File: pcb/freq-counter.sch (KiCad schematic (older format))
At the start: 64 parts, among them J1 RPM on board, J10 Power-Terminal0, J11 Hz/RPM_Terminal1, J12 Hz/RPM_Terminal0, J13 1kMG_Terminal1, J14 1kMG_Terminal0, J2 BNC, J3 RPM to Board, J4 Jack-DC, J5 Segments-Terminal0, J6 Digits-Terminal0, J7 Segments-Terminal1, J8 Digits-Terminal1, J9 Power-Terminal1, Q1 CSC388A, Q2 CSC388A, Q3 2SA1015, Q4 2SC1815, Q5 2SC1815, SW1 on/off, SW2 count up, SW3 toggle, SW4 SW_SIGNAL, U1 SN74HC02N, U2 ATTINY4313-PU(freq-counter), U3 EE-SX460, Y1 10MHz

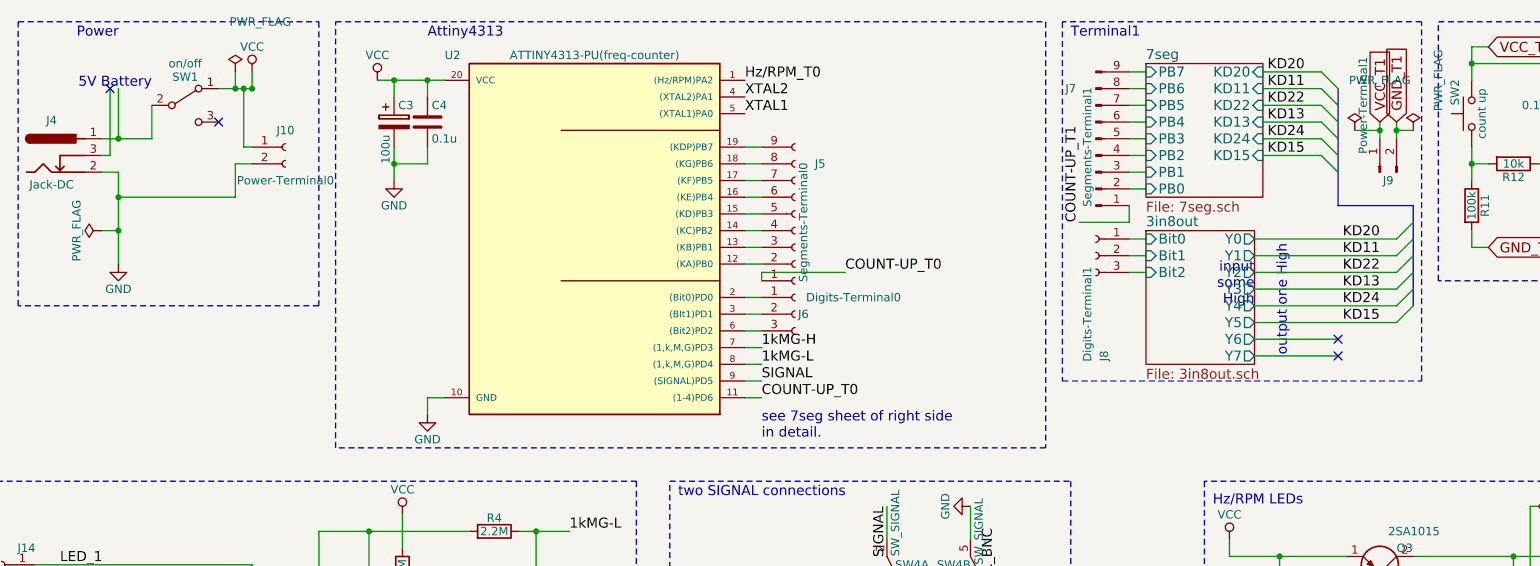
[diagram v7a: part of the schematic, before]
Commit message: Power-Digtis_Terminal1 を作成。Power, Digits の Terminal1 を連結させた。
Connectors_JSTを使っても取り外しを出来るのは，
１階と２階の基板を離してからだと思ったので近くにいた，Digits系と繋げてしまった。
こっちの方が強度を出せると思うため。
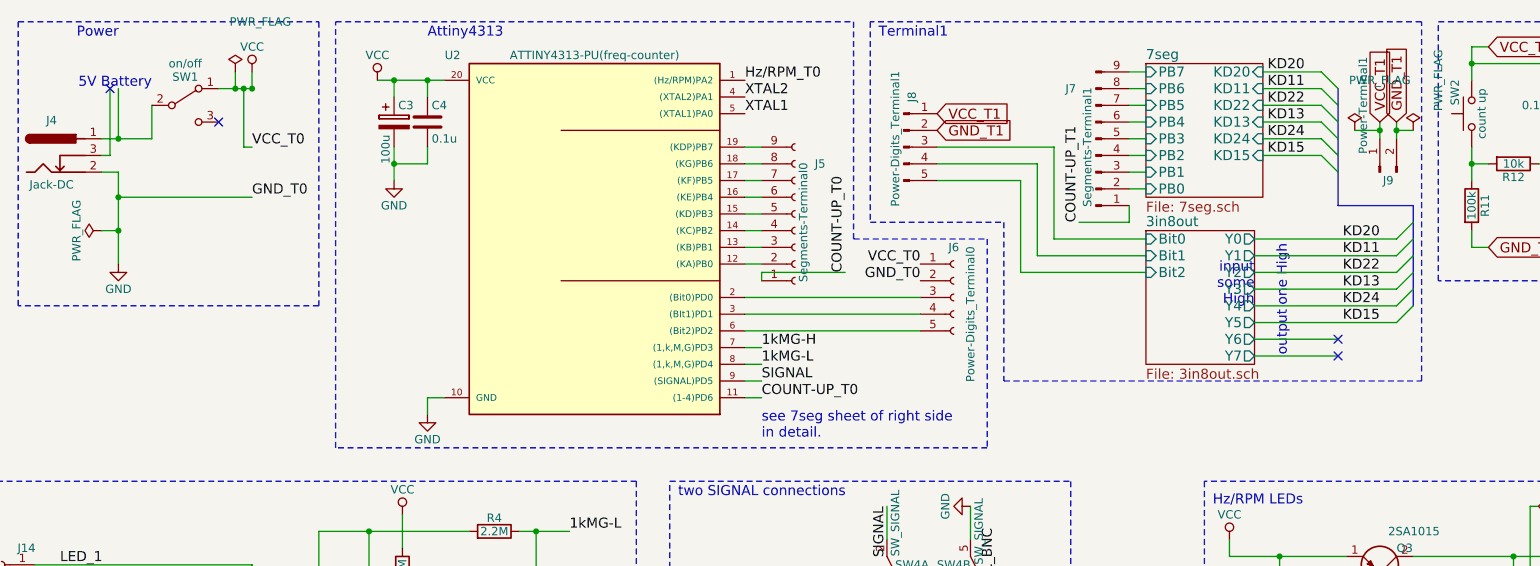
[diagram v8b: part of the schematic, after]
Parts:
- removed J10: Power-Terminal0, Conn_JST:JST_XH_B02B-XH-A_1x02_P2.50mm_Horizontal, symbol Conn_01x02_Female
- removed J6: Digits-Terminal0, Connector_PinSocket_2.54mm:PinSocket_1x03_P2.54mm_Vertical, symbol Conn_01x03_Female
- removed J8: Digits-Terminal1, Connector_PinHeader_2.54mm:PinHeader_1x03_P2.54mm_Vertical, symbol Conn_01x03_Female
- added J6: Power-Digits_Terminal0, Connector_PinSocket_2.54mm:PinSocket_1x05_P2.54mm_Vertical, symbol Conn_01x05_Female
- added J8: Power-Digits_Terminal1, Connector_PinHeader_2.54mm:PinHeader_1x05_P2.54mm_Vertical, symbol Conn_01x05_Male
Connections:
- net 3in8out/Bit0: now also J8.3 (Pin_3)
- net 3in8out/Bit1: now also J8.4 (Pin_4)
- net 3in8out/Bit2: now also J8.5 (Pin_5)
- net GND: now also J6.2 (Pin_2)
- net GND_T1: now also J8.2 (Pin_2)
- net VCC: now also J6.1 (Pin_1)
- net VCC_T1: now also J8.1 (Pin_1)
- net at U2.2 ((Bit0)PD0): now also J6.3 (Pin_3)
- net at U2.3 ((BIt1)PD1): now also J6.4 (Pin_4)
- net at U2.6 ((Bit2)PD2): now also J6.5 (Pin_5)
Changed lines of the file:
@@
 $EndComp
 $Comp
-L GND #PWR01
+L GND #PWR4
 U 1 1 5A10C10B
 P 1450 5100
-F 0 "#PWR01" H 1450 4850 50  0001 C CNN
+F 0 "#PWR4" H 1450 4850 50  0001 C CNN
 F 1 "GND" H 1450 4950 50  0000 C CNN
 F 2 "" H 1450 5100 50  0001 C CNN
@@
 $EndComp
 $Comp
-L GND #PWR02
+L GND #PWR13
 U 1 1 5A102C86
 P 5050 6000
-F 0 "#PWR02" H 5050 5750 50  0001 C CNN
+F 0 "#PWR13" H 5050 5750 50  0001 C CNN
 F 1 "GND" H 5050 5850 50  0000 C CNN
 F 2 "" H 5050 6000 50  0001 C CNN
@@
 $EndComp
 $Comp
-L GND #PWR03
+L GND #PWR3
 U 1 1 5A14ACE7
 P 1250 2200
-F 0 "#PWR03" H 1250 1950 50  0001 C CNN
+F 0 "#PWR3" H 1250 1950 50  0001 C CNN
 F 1 "GND" H 1250 2050 50  0000 C CNN
 F 2 "" H 1250 2200 50  0001 C CNN
@@
 $EndComp
 $Comp
-L PWR_FLAG #FLG04
+L PWR_FLAG #FLG1
 U 1 1 5A14B084
 P 1150 2000
-F 0 "#FLG04" H 1150 2075 50  0001 C CNN
+F 0 "#FLG1" H 1150 2075 50  0001 C CNN
 F 1 "PWR_FLAG" H 1150 2150 50  0000 C CNN
 F 2 "" H 1150 2000 50  0001 C CNN
@@
 $EndComp
 $Comp
-L PWR_FLAG #FLG05
+L PWR_FLAG #FLG2
 U 1 1 5A14B889
 P 1950 1050
-F 0 "#FLG05" H 1950 1125 50  0001 C CNN
+F 0 "#FLG2" H 1950 1125 50  0001 C CNN
 F 1 "PWR_FLAG" H 2100 1350 50  0000 C CNN
 F 2 "" H 1950 1050 50  0001 C CNN
@@
 $EndComp
 $Comp
-L GND #PWR06
+L GND #PWR8
 U 1 1 5A14CF4C
 P 2900 1700
-F 0 "#PWR06" H 2900 1450 50  0001 C CNN
+F 0 "#PWR8" H 2900 1450 50  0001 C CNN
 F 1 "GND" H 2900 1550 50  0000 C CNN
 F 2 "" H 2900 1700 50  0001 C CNN
@@
 Power
 $Comp
-L PWR_FLAG #FLG07
+L PWR_FLAG #FLG4
 U 1 1 5A15C58C
 P 5500 5050
-F 0 "#FLG07" H 5500 5125 50  0001 C CNN
+F 0 "#FLG4" H 5500 5125 50  0001 C CNN
 F 1 "PWR_FLAG" H 5450 5200 50  0000 C CNN
 F 2 "" H 5500 5050 50  0001 C CNN
@@
 $EndComp
 $Comp
-L PWR_FLAG #FLG08
+L PWR_FLAG #FLG3
 U 1 1 5A15C934
 P 5450 5400
-F 0 "#FLG08" H 5450 5475 50  0001 C CNN
+F 0 "#FLG3" H 5450 5475 50  0001 C CNN
 F 1 "PWR_FLAG" V 5350 5400 50  0000 C CNN
 F 2 "" H 5450 5400 50  0001 C CNN
@@
 NoConn ~ 1200 1150
 $Comp
-L VCC #PWR09
+L VCC #PWR5
 U 1 1 5A193502
 P 2050 1050
-F 0 "#PWR09" H 2050 900 50  0001 C CNN
+F 0 "#PWR5" H 2050 900 50  0001 C CNN
 F 1 "VCC" H 2050 1200 50  0000 C CNN
 F 2 "" H 2050 1050 50  0001 C CNN
@@
 Text Label 6400 4500 0    60   ~ 0
 GND_BNC
-$Comp
-L Conn_01x03_Female J6
-U 1 1 5A1E8B3E
-P 5300 2500
-F 0 "J6" H 5350 2500 50  0000 C CNN
-F 1 "Digits-Terminal0" H 5650 2600 50  0000 C CNN
-F 2 "Connector_PinSocket_2.54mm:PinSocket_1x03_P2.54mm_Vertical" H 5300 2500 50  0001 C CNN
-F 3 "" H 5300 2500 50  0001 C CNN
-	1    5300 2500
-	1    0    0    -1
-$EndComp
-$Comp
-L Conn_01x03_Female J8
-U 1 1 5A1EAFDB
-P 7100 2150
-F 0 "J8" V 7050 1550 50  0000 C CNN
-F 1 "Digits-Terminal1" V 7150 1800 50  0000 C CNN
-F 2 "Connector_PinHeader_2.54mm:PinHeader_1x03_P2.54mm_Vertical" H 7100 2150 50  0001 C CNN
-F 3 "" H 7100 2150 50  0001 C CNN
-	1    7100 2150
-	-1   0    0    -1
-$EndComp
-Text Notes 6950 850  0    60   ~ 0
+Text Notes 5800 850  0    60   ~ 0
 Terminal1
 $Comp
@@
 GND_T1
 $Comp
-L Conn_01x02_Female J10
-U 1 1 5A202C49
-P 2250 1500
-F 0 "J10" H 2250 1600 50  0000 C CNN
-F 1 "Power-Terminal0" H 2250 1300 50  0000 C CNN
-F 2 "Conn_JST:JST_XH_B02B-XH-A_1x02_P2.50mm_Horizontal" H 2250 1500 50  0001 C CNN
-F 3 "" H 2250 1500 50  0001 C CNN
-	1    2250 1500
-	1    0    0    -1
-$EndComp
-$Comp
-L VCC #PWR010
+L VCC #PWR7
 U 1 1 5A20AA1B
 P 2800 1100
-F 0 "#PWR010" H 2800 950 50  0001 C CNN
+F 0 "#PWR7" H 2800 950 50  0001 C CNN
 F 1 "VCC" H 2800 1250 50  0000 C CNN
 F 2 "" H 2800 1100 50  0001 C CNN
@@
 VCC_T1
 $Comp
-L PWR_FLAG #FLG011
+L PWR_FLAG #FLG6
 U 1 1 5A1E7BBB
 P 9000 1400
-F 0 "#FLG011" H 9000 1475 50  0001 C CNN
+F 0 "#FLG6" H 9000 1475 50  0001 C CNN
 F 1 "PWR_FLAG" V 9150 1700 50  0000 C CNN
 F 2 "" H 9000 1400 50  0001 C CNN
@@
 $EndComp
 $Comp
-L PWR_FLAG #FLG012
+L PWR_FLAG #FLG5
 U 1 1 5A1E8382
 P 8650 1400
-F 0 "#FLG012" H 8650 1475 50  0001 C CNN
+F 0 "#FLG5" H 8650 1475 50  0001 C CNN
 F 1 "PWR_FLAG" H 8800 1700 50  0000 C CNN
 F 2 "" H 8650 1400 50  0001 C CNN
@@
 $EndComp
 $Comp
-L VCC #PWR013
+L VCC #PWR2
 U 1 1 5A1EAB1C
 P 1000 4500
-F 0 "#PWR013" H 1000 4350 50  0001 C CNN
+F 0 "#PWR2" H 1000 4350 50  0001 C CNN
 F 1 "VCC" H 1000 4650 50  0000 C CNN
 F 2 "" H 1000 4500 50  0001 C CNN
@@
 $EndComp
 $Comp
-L GND #PWR014
+L GND #PWR11
 U 1 1 5A1EBF20
 P 3100 3100
-F 0 "#PWR014" H 3100 2850 50  0001 C CNN
+F 0 "#PWR11" H 3100 2850 50  0001 C CNN
 F 1 "GND" H 3100 2950 50  0000 C CNN
 F 2 "" H 3100 3100 50  0001 C CNN
@@
 $EndComp
 $Comp
-L GND #PWR015
+L GND #PWR6
 U 1 1 5A1ECBC1
 P 2450 6400
-F 0 "#PWR015" H 2450 6150 50  0001 C CNN
+F 0 "#PWR6" H 2450 6150 50  0001 C CNN
 F 1 "GND" H 2450 6250 50  0000 C CNN
 F 2 "" H 2450 6400 50  0001 C CNN
@@
 $EndComp
 $Comp
-L GND #PWR016
+L GND #PWR1
 U 1 1 5A1ED93F
 P 850 4550
-F 0 "#PWR016" H 850 4300 50  0001 C CNN
+F 0 "#PWR1" H 850 4300 50  0001 C CNN
 F 1 "GND" H 850 4400 50  0000 C CNN
 F 2 "" H 850 4550 50  0001 C CNN
@@
 $EndComp
 $Comp
-L GND #PWR017
+L GND #PWR10
 U 1 1 5A1EE509
 P 2950 4800
-F 0 "#PWR017" H 2950 4550 50  0001 C CNN
+F 0 "#PWR10" H 2950 4550 50  0001 C CNN
 F 1 "GND" H 2950 4650 50  0000 C CNN
 F 2 "" H 2950 4800 50  0001 C CNN
@@
 $EndComp
 $Comp
-L VCC #PWR018
+L VCC #PWR12
 U 1 1 5A1EEDD1
 P 3100 5250
-F 0 "#PWR018" H 3100 5100 50  0001 C CNN
+F 0 "#PWR12" H 3100 5100 50  0001 C CNN
 F 1 "VCC" H 3100 5400 50  0000 C CNN
 F 2 "" H 3100 5250 50  0001 C CNN
@@
 $EndComp
 $Comp
-L VCC #PWR019
+L VCC #PWR9
 U 1 1 5A1EFB20
 P 2950 3700
-F 0 "#PWR019" H 2950 3550 50  0001 C CNN
+F 0 "#PWR9" H 2950 3550 50  0001 C CNN
 F 1 "VCC" H 2950 3850 50  0000 C CNN
 F 2 "" H 2950 3700 50  0001 C CNN
@@
 $EndComp
 $Comp
-L GND #PWR020
+L GND #PWR17
 U 1 1 5A1F0879
 P 7900 6150
-F 0 "#PWR020" H 7900 5900 50  0001 C CNN
+F 0 "#PWR17" H 7900 5900 50  0001 C CNN
 F 1 "GND" H 7900 6000 50  0000 C CNN
 F 2 "" H 7900 6150 50  0001 C CNN
@@
 $EndComp
 $Comp
-L VCC #PWR021
+L VCC #PWR16
 U 1 1 5A1F0C13
 P 7900 3850
-F 0 "#PWR021" H 7900 3700 50  0001 C CNN
+F 0 "#PWR16" H 7900 3700 50  0001 C CNN
 F 1 "VCC" H 7900 4000 50  0000 C CNN
 F 2 "" H 7900 3850 50  0001 C CNN
@@
 $EndComp
 $Comp
-L GND #PWR022
+L GND #PWR15
 U 1 1 5A1F3CDE
 P 6350 3650
-F 0 "#PWR022" H 6350 3400 50  0001 C CNN
+F 0 "#PWR15" H 6350 3400 50  0001 C CNN
 F 1 "GND" H 6350 3500 50  0000 C CNN
 F 2 "" H 6350 3650 50  0001 C CNN
@@
 $EndComp
 $Comp
-L VCC #PWR023
+L VCC #PWR14
 U 1 1 5A1F4C25
 P 5800 4400
-F 0 "#PWR023" H 5800 4250 50  0001 C CNN
+F 0 "#PWR14" H 5800 4250 50  0001 C CNN
 F 1 "VCC" H 5800 4550 50  0000 C CNN
 F 2 "" H 5800 4400 50  0001 C CNN
@@
 	5000 2700 5100 2700
 Wire Wire Line
-	7300 2250 7400 2250
-Wire Wire Line
-	7300 2050 7400 2050
-Wire Wire Line
-	7300 2150 7400 2150
+	6650 2250 7400 2250
+Wire Wire Line
+	6850 2050 7400 2050
+Wire Wire Line
+	6750 2150 7400 2150
 Wire Wire Line
 	7300 1750 7400 1750
@@
 	9350 2000 9350 2100
 Wire Notes Line
-	6800 3300 2550 3300
+	6450 3300 2550 3300
 Wire Notes Line
 	2550 3300 2550 750
 Wire Notes Line
-	2550 750  6800 750
-Wire Notes Line
-	6800 750  6800 3300
+	2550 750  5650 750
 Wire Wire Line
 	5250 6400 5200 6400
@@
 	5000 2200 5100 2200
 Wire Wire Line
-	5100 2400 5000 2400
-Wire Wire Line
-	5000 2500 5100 2500
-Wire Wire Line
-	5100 2600 5000 2600
+	6050 2400 5000 2400
+Wire Wire Line
+	5000 2500 6050 2500
+Wire Wire Line
+	6050 2600 5000 2600
 Wire Wire Line
 	8550 2750 8050 2750
 Wire Notes Line
-	6900 750  6900 2900
-Wire Notes Line
-	6900 2900 9050 2900
+	6550 2900 9050 2900
 Wire Notes Line
 	9050 2900 9050 750
 Wire Notes Line
-	9050 750  6900 750
+	9050 750  5750 750
 Wire Wire Line
 	8800 1350 8800 1450
@@
 Connection ~ 2000 1150
 Wire Wire Line
-	2050 1600 1950 1600
-Wire Wire Line
-	1950 1600 1950 1800
-Wire Wire Line
-	1950 1800 1250 1800
+	1250 1800 2050 1800
 Connection ~ 1250 1800
 Wire Wire Line
@@
 Text Label 5100 3000 0    60   ~ 0
 COUNT-UP_T0
-Text Label 5600 2250 0    60   ~ 0
+Text Label 5600 2250 1    60   ~ 0
 COUNT-UP_T0
 Wire Wire Line
@@
 Wire Wire Line
 	2250 5700 2250 5500
+$Comp
+L Conn_01x05_Female J6
+U 1 1 5A237074
+P 6250 2400
+F 0 "J6" H 6250 2700 50  0000 C CNN
+F 1 "Power-Digits_Terminal0" V 6350 2300 50  0000 C CNN
+F 2 "Connector_PinSocket_2.54mm:PinSocket_1x05_P2.54mm_Vertical" H 6250 2400 50  0001 C CNN
+F 3 "" H 6250 2400 50  0001 C CNN
+	1    6250 2400
+	1    0    0    -1
+$EndComp
+Text Label 2050 1500 0    60   ~ 0
+VCC_T0
+Text Label 2050 1800 0    60   ~ 0
+GND_T0
+Text Label 6050 2200 2    60   ~ 0
+VCC_T0
+Text Label 6050 2300 2    60   ~ 0
+GND_T0
+Wire Notes Line
+	5650 750  5650 2050
+Wire Notes Line
+	5650 2050 6450 2050
+Wire Notes Line
+	6450 2050 6450 3300
+$Comp
+L Conn_01x05_Male J8
+U 1 1 5A23DE56
+P 5950 1500
+F 0 "J8" V 6000 1800 50  0000 C CNN
+F 1 "Power-Digits_Terminal1" V 5900 1550 50  0000 C CNN
+F 2 "Connector_PinHeader_2.54mm:PinHeader_1x05_P2.54mm_Vertical" H 5950 1500 50  0001 C CNN
+F 3 "" H 5950 1500 50  0001 C CNN
+	1    5950 1500
+	1    0    0    -1
+$EndComp
+Text GLabel 6150 1300 2    60   Input ~ 0
+VCC_T1
+Text GLabel 6150 1400 2    60   Input ~ 0
+GND_T1
+Wire Wire Line
+	6150 1500 6850 1500
+Wire Wire Line
+	6850 1500 6850 2050
+Wire Wire Line
+	6150 1600 6750 1600
+Wire Wire Line
+	6750 1600 6750 2150
+Wire Wire Line
+	6650 2250 6650 1700
+Wire Wire Line
+	6650 1700 6150 1700
+Wire Notes Line
+	5750 750  5750 1950
+Wire Notes Line
+	5750 1950 6550 1950
+Wire Notes Line
+	6550 1950 6550 2900
 $EndSCHEMATC
